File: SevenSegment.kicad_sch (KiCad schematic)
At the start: 51 parts, among them J1 Conn_02x04_Odd_Even, SW2 SW_Push, U1 W25Q16JVUXIQ, U2 RP2040, Y1 12.000MHz

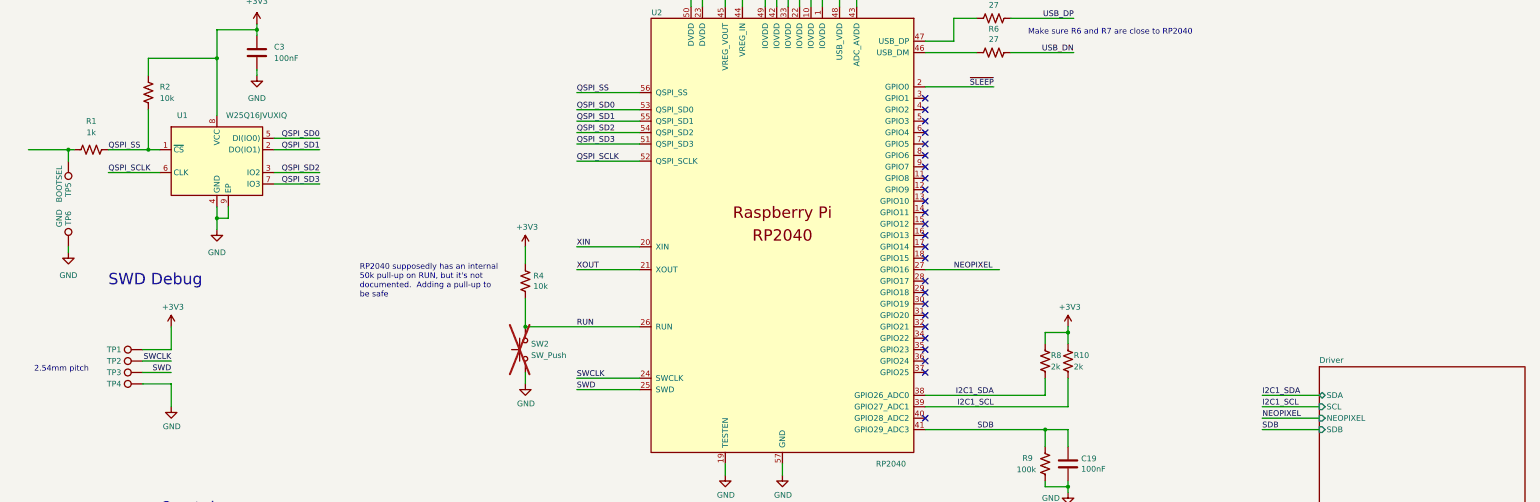
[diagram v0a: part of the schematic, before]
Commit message: Update design
New features:
* Power switch for NEOPIXEL to save power when sleeping
* Level translator from 3.3V to 5V for neopixel for hygiene
* Use "real" DIP switch footprint for debug/boot buttons, even
  if this is going to be unpopulated in practice, since both
  these modes can be entered via software.  Still can be populated
  for debugging!
* Removed unnecessary RESET switch footprint.

Some additional notes added to v1-notes.txt about other tweaks that
might still be needed before a v2.
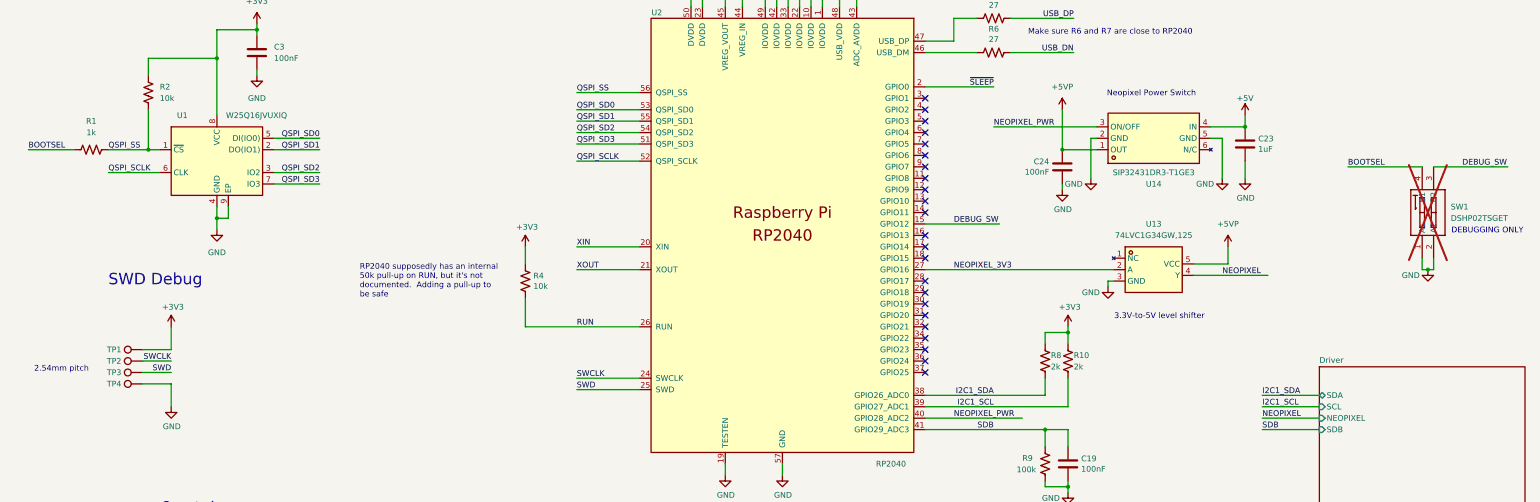
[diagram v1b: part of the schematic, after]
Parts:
- removed SW2: SW_Push, Button_Switch_SMD:SW_SPST_CK_KXT3, symbol Switch:SW_Push
- removed TP5: BOOTSEL, TestPoint:TestPoint_Pad_D1.0mm, symbol Connector:TestPoint
- removed TP6: GND, TestPoint:TestPoint_Pad_D1.0mm, symbol Connector:TestPoint
- added C23: 1uF, Capacitor_SMD:C_0402_1005Metric, symbol Device:C
- added C24: 100nF, Capacitor_SMD:C_0402_1005Metric, symbol Device:C
- added SW1: DSHP02TSGET, LCSC:SW-SMD_4P_DSHP02TSGET, symbol LCSC:DSHP02TSGET
- added U13: 74LVC1G34GW,125, LCSC:SOT-353_L2.1-W1.3-P0.65-LS2.3-BR, symbol LCSC:74LVC1G34GW,125
- added U14: SIP32431DR3-T1GE3, LCSC:SOT-363_L2.0-W1.3-P0.65-LS2.1-BR, symbol LCSC:SIP32431DR3-T1GE3
- U2: symbol MCU_RaspberryPi_RP2040:RP2040 -> LEDMatrix:RP2040
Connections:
- net +5V: now also C23.1, U14.4 (IN)
- net GND: now also C23.2, C24.2, SW1.1 (A1), SW1.2 (A2), U13.3 (GND), U14.2 (GND), U14.5 (GND)
- net NEOPIXEL: now also U13.4 (Y); no longer U2.27 (GPIO16)
- net BOOTSEL: now reaches R1.1
- net BOOTSEL: now also SW1.4 (B1)
- net DEBUG_SW: now reaches U2.15 (GPIO12)
- net DEBUG_SW: now also SW1.3 (B2)
- net NEOPIXEL_PWR: now reaches U2.40 (GPIO28_ADC2)
- net NEOPIXEL_PWR: now also U14.3 (ON/OFF)
- new net +5VP: C24.1, U13.5 (VCC), U14.1 (OUT)
- new net NEOPIXEL_3V3: U13.2 (A), U2.27 (GPIO16)
- no-connect marks 25 -> 23
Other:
- note added: "3.3V-to-5V level shifter"
- note added: "DEBUGGING ONLY"
- note added: "Neopixel Power Switch"
